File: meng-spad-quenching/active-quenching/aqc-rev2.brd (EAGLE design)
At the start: 120 x 74.9 mm, 297 parts, among them IC1 ADCMP582, IC10 74AHC1G04DBV, IC11 74AHC1G04DBV, IC12 TLV272DGK, IC13 TLV271DBV, IC14 74AHC1G04DBV, IC15 ALD1106, IC16 ALD1107, IC17 74AHC1G04DBV, IC18 LT1534-1, IC19 LT1534-1, IC2 TLV271DBV, IC20 STM32F411RE, IC22 TPS7A3001, IC24 TPS7A4901, IC25 TPS7A4901, IC27 USBLC6-2SC6Y, IC28 MAX572X, IC3 NC7SV74K8X, IC4 TLV272DGK, IC5 NC7WZ16P6X, IC6 LTC1711, IC7 DS1100LU-20+, IC8 LM1117, M1 BSS806N, M2 BSS806N, M3 BSS806N, Q1 IRLML6402TRPBF, Q2 MMBTH81, Q3 MMBTH81, Q5 MMBTH81, Q7 MMBTH81, Q8 MMBTH81, SW1 MCU_RST, T1 MMBTH10, T2 MMBTH10, T5 MMBTH10, T6 MMBTH10, T7 MMBTH10, T8 MMBTH10, T9 MMBTH10, U1 SN65EPT21DGK, U2 SN65EPT22DGK, X1 CONN_SPAD, X2 CONN_PHOTON_COUNTER, X3 KEYSTONE-7774, X4 KEYSTONE-7774, X5 CONN_SMU, X6 CONN_FORCE_QUENCH, X7 CONN_PULLDN_SENSE, X8 PN61729-S

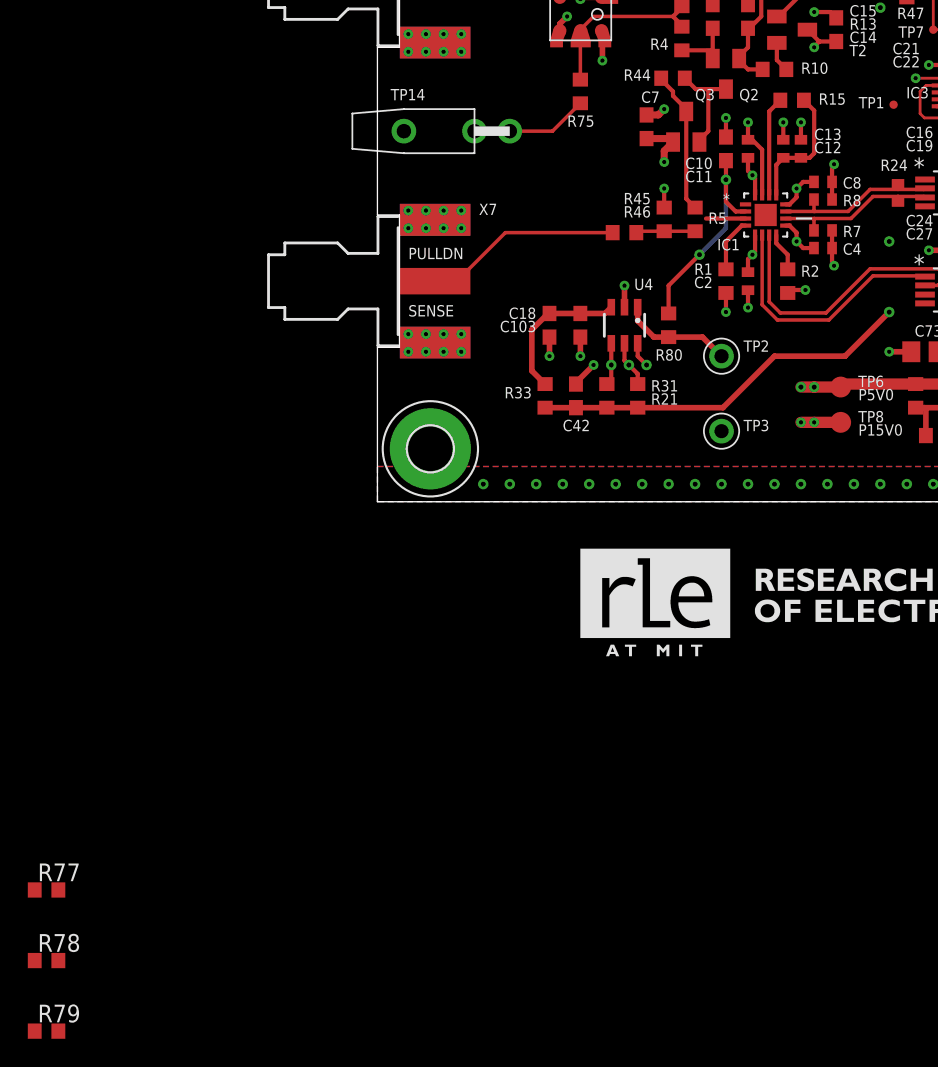
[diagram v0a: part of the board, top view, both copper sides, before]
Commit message: Placed and routed RC filter option
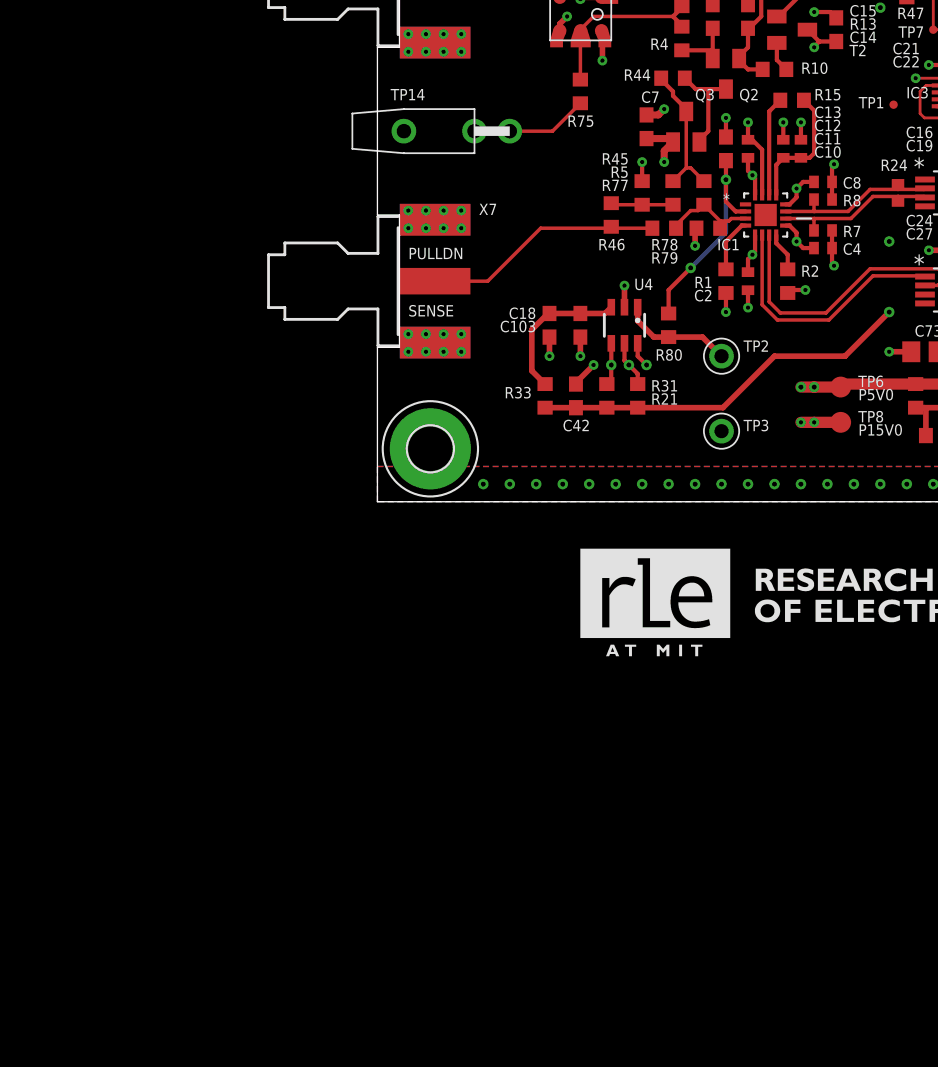
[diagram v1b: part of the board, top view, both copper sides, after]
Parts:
- moved R79 74.9 mm to (23.8, 19.7)
- moved R77 69.0 mm to (23.5, 22.2), turned to 90 degrees
- moved R78 68.9 mm to (20.6, 19.7)
- moved R45 2.48 mm to (19.1, 22.2)
- moved R5 2.48 mm to (21.3, 22.2)
- moved R46 1.59 mm to (16.8, 20.6), turned to 90 degrees
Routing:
- net SPAD_PULLDN_SENSE: track 2.85 -> 6.91 mm
- net N$32: track 14.2 -> 17.3 mm
- net GND: track 329.7 -> 331.0 mm, vias 357 -> 358

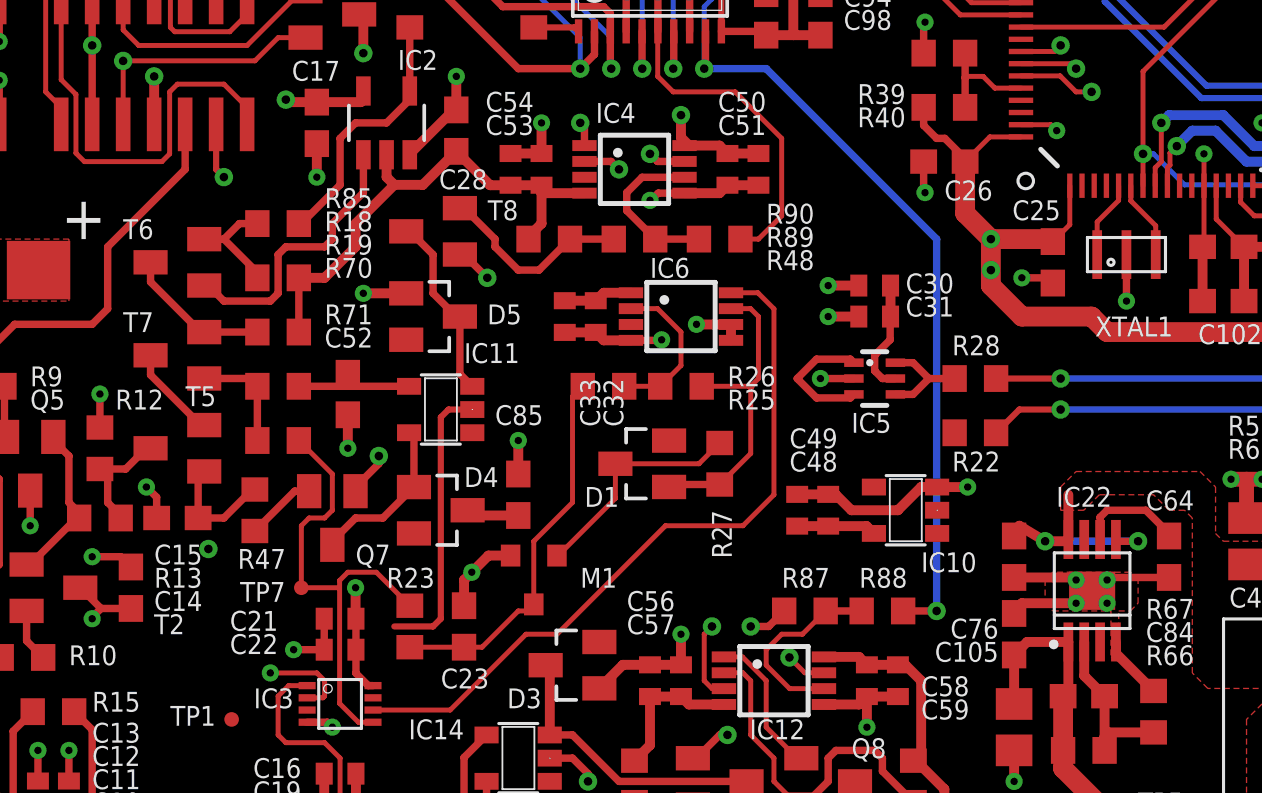
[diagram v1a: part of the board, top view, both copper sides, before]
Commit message: Misc routing, connected -5V to LDO output
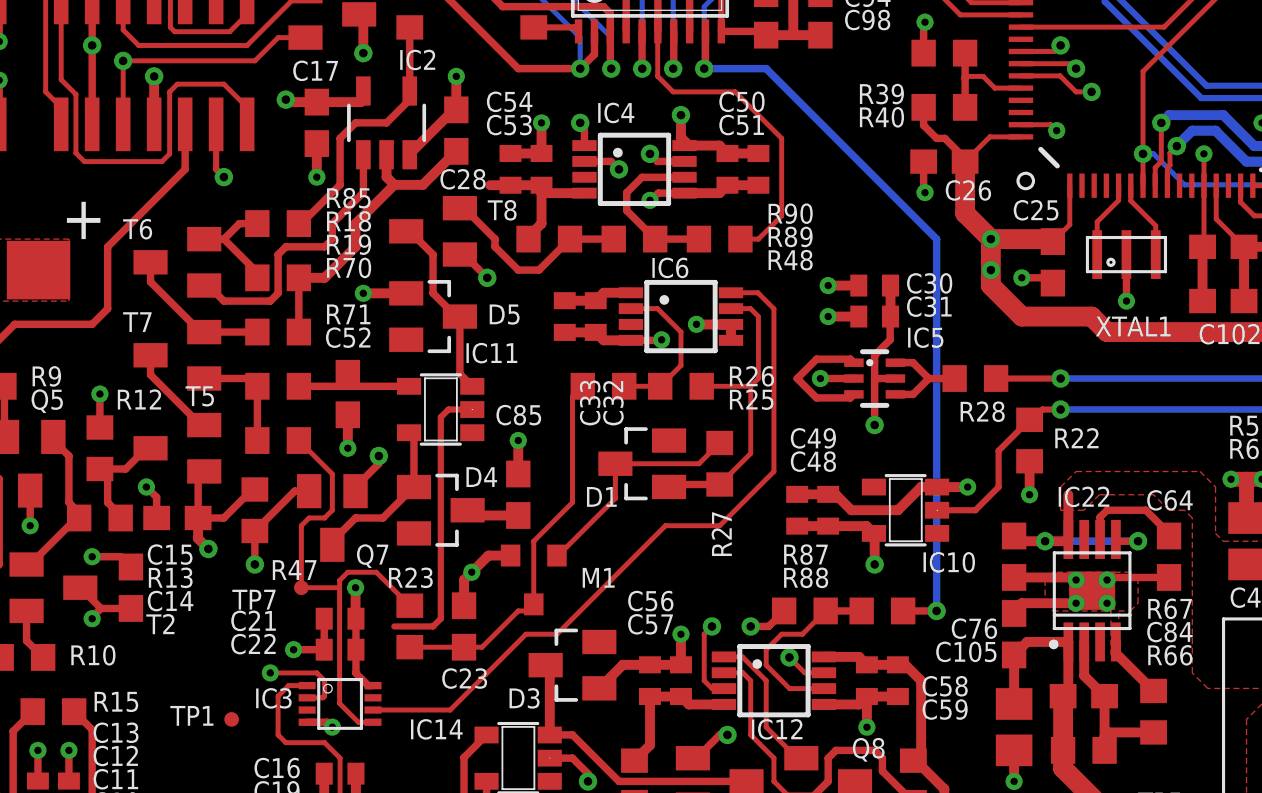
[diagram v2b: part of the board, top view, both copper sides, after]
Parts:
- moved R22 2.25 mm to (69.8, 40.0), turned to 90 degrees
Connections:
- net PP_N5V0: no longer C28.1, IC2.2, R18.1, R19.1
- net PP_N5V0_ANALOG: now also C28.1, IC2.2, R18.1, R19.1
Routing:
- net N$1: track 4.45 -> 29.5 mm, vias 1 -> 2
- net PP_N5V0: track 36.5 -> 21.7 mm
- net PP_P3V3: track 357.8 -> 371.9 mm, vias 16 -> 18
- net PP_N5V0_ANALOG: track 12.3 -> 25.1 mm
- net FORCE_QUENCH: track 71.9 -> 76.5 mm
- net PP_P5V0_ANALOG: track 192.6 -> 191.0 mm
- net GND: track 331.0 -> 332.4 mm, vias 358 -> 359
- net !ONE_SHOT_CLR: track 29.7 -> 29.2 mm

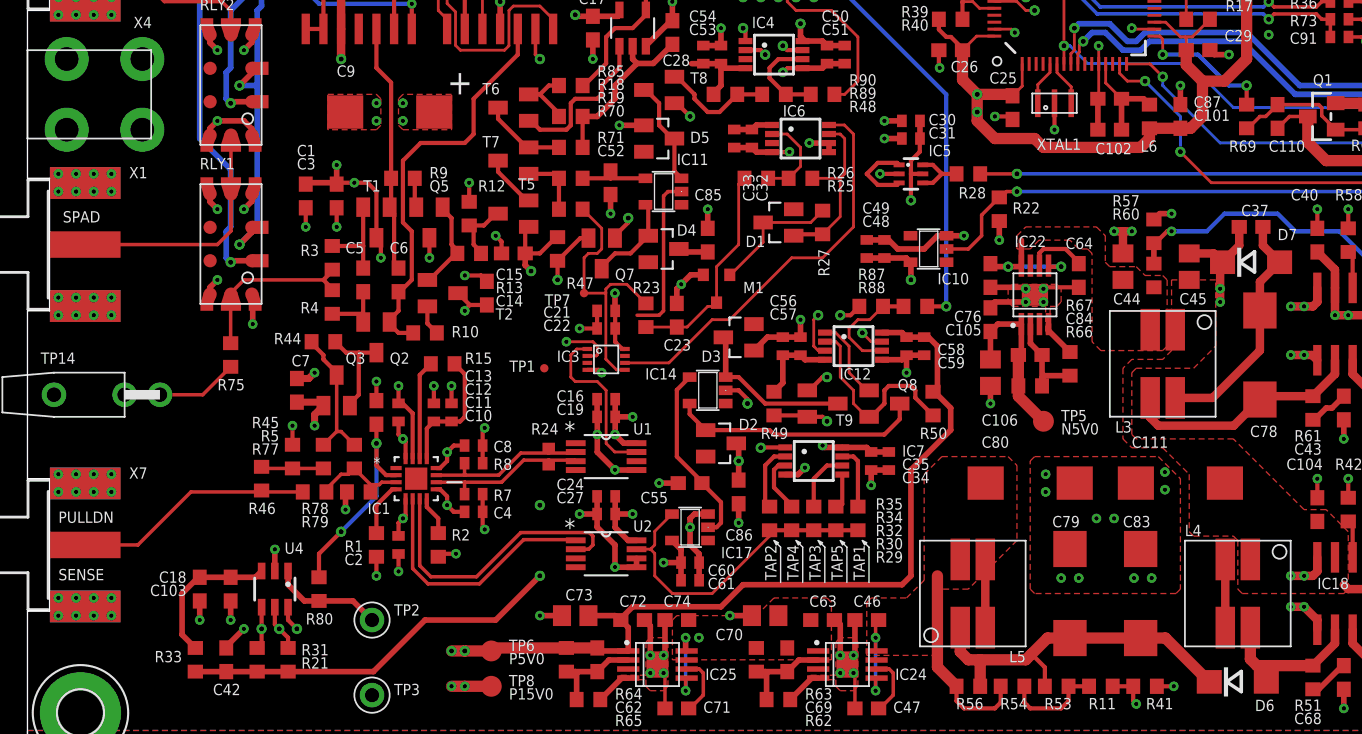
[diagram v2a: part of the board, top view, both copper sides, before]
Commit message: Routed relay power trace
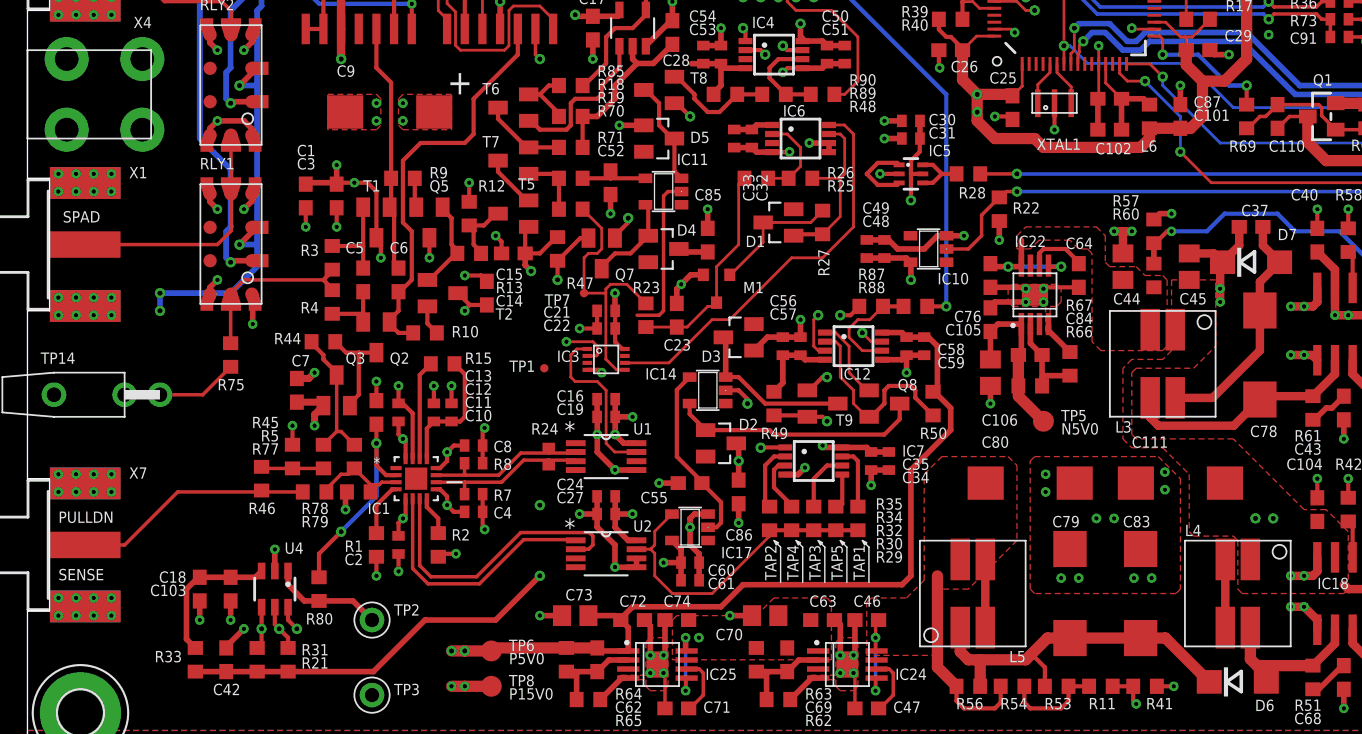
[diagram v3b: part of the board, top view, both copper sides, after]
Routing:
- net SMPS_USB_VDD: track 120.9 -> 253.9 mm, vias 6 -> 10
- net DAC2_SCL: track 162.3 -> 160.9 mm
- net DAC2_ADDRSEL: track 163.2 -> 161.8 mm
- net DAC2_SDA: track 160.6 -> 159.2 mm
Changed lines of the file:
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@@
 <contactref element="R78" pad="1"/>
 <wire x1="16.861078125" y1="19.685" x2="19.7875" y2="19.685" width="0.254" layer="1"/>
-<wire x1="16.861078125" y1="19.685" x2="11.7475" y2="19.685" width="0.254" layer="1"/>
-<wire x1="11.7475" y1="19.685" x2="7.9375" y2="15.875" width="0.254" layer="1"/>
-<wire x1="7.9375" y1="15.875" x2="4.1529" y2="15.875" width="0.254" layer="1"/>
+<wire x1="16.861078125" y1="19.685" x2="10.795" y2="19.685" width="0.254" layer="1"/>
+<wire x1="10.795" y1="19.685" x2="6.985" y2="15.875" width="0.254" layer="1"/>
+<wire x1="6.985" y1="15.875" x2="4.1529" y2="15.875" width="0.254" layer="1"/>
 <wire x1="16.8275" y1="19.7875" x2="16.8275" y2="19.718578125" width="0.254" layer="1"/>
 <wire x1="16.8275" y1="19.718578125" x2="16.861078125" y2="19.685" width="0.254" layer="1"/>
@@
 <wire x1="16.38" y1="13.55" x2="16.83" y2="14" width="0.4064" layer="1"/>
 <wire x1="12.3825" y1="13.55" x2="12.28" y2="13.55" width="0.4064" layer="1"/>
-<wire x1="12.28" y1="13.55" x2="11.1125" y2="12.3825" width="0.4064" layer="1"/>
-<wire x1="11.1125" y1="12.3825" x2="11.1125" y2="9.4225" width="0.4064" layer="1"/>
-<wire x1="11.1125" y1="9.4225" x2="12.065" y2="8.47" width="0.4064" layer="1"/>
+<wire x1="12.28" y1="13.55" x2="11.43" y2="12.7" width="0.4064" layer="1"/>
+<wire x1="11.43" y1="12.7" x2="11.43" y2="9.105" width="0.4064" layer="1"/>
+<wire x1="11.43" y1="9.105" x2="12.065" y2="8.47" width="0.4064" layer="1"/>
 </signal>
 <signal name="MCU_VCAP_2">
@@
 <wire x1="66.675" y1="71.12" x2="13.0175" y2="71.12" width="0.2032" layer="15"/>
 <wire x1="13.0175" y1="71.12" x2="12.3825" y2="70.485" width="0.2032" layer="15"/>
-<wire x1="12.3825" y1="17.78" x2="10.16" y2="15.5575" width="0.2032" layer="15"/>
-<wire x1="10.16" y1="15.5575" x2="10.16" y2="5.715" width="0.2032" layer="15"/>
-<wire x1="10.16" y1="5.715" x2="11.43" y2="4.445" width="0.2032" layer="15"/>
-<wire x1="11.43" y1="4.445" x2="16.1925" y2="4.445" width="0.2032" layer="15"/>
-<wire x1="16.1925" y1="4.445" x2="17.4625" y2="5.715" width="0.2032" layer="15"/>
+<wire x1="12.3825" y1="17.145" x2="10.795" y2="15.5575" width="0.2032" layer="15"/>
+<wire x1="10.795" y1="15.5575" x2="10.795" y2="5.715" width="0.2032" layer="15"/>
+<wire x1="10.795" y1="5.715" x2="11.43" y2="5.08" width="0.2032" layer="15"/>
+<wire x1="11.43" y1="5.08" x2="16.8275" y2="5.08" width="0.2032" layer="15"/>
+<wire x1="16.8275" y1="5.08" x2="17.4625" y2="5.715" width="0.2032" layer="15"/>
 <wire x1="17.4625" y1="5.715" x2="17.4625" y2="9.2075" width="0.2032" layer="15"/>
 <wire x1="17.4625" y1="9.2075" x2="16.8275" y2="9.8425" width="0.2032" layer="15"/>
-<wire x1="12.3825" y1="70.485" x2="12.3825" y2="17.78" width="0.2032" layer="15"/>
+<wire x1="12.3825" y1="70.485" x2="12.3825" y2="17.145" width="0.2032" layer="15"/>
 </signal>
 <signal name="DAC2_SCL">
@@
 <wire x1="11.7475" y1="70.8025" x2="12.7" y2="71.755" width="0.2032" layer="15"/>
 <wire x1="18.0975" y1="9.8425" x2="18.0975" y2="5.3975" width="0.2032" layer="15"/>
-<wire x1="18.0975" y1="5.3975" x2="16.51" y2="3.81" width="0.2032" layer="15"/>
-<wire x1="16.51" y1="3.81" x2="11.1125" y2="3.81" width="0.2032" layer="15"/>
-<wire x1="11.1125" y1="3.81" x2="9.525" y2="5.3975" width="0.2032" layer="15"/>
-<wire x1="9.525" y1="5.3975" x2="9.525" y2="15.875" width="0.2032" layer="15"/>
-<wire x1="9.525" y1="15.875" x2="11.7475" y2="18.0975" width="0.2032" layer="15"/>
-<wire x1="11.7475" y1="18.0975" x2="11.7475" y2="70.8025" width="0.2032" layer="15"/>
+<wire x1="18.0975" y1="5.3975" x2="17.145" y2="4.445" width="0.2032" layer="15"/>
+<wire x1="17.145" y1="4.445" x2="11.1125" y2="4.445" width="0.2032" layer="15"/>
+<wire x1="11.1125" y1="4.445" x2="10.16" y2="5.3975" width="0.2032" layer="15"/>
+<wire x1="10.16" y1="5.3975" x2="10.16" y2="15.875" width="0.2032" layer="15"/>
+<wire x1="10.16" y1="15.875" x2="11.7475" y2="17.4625" width="0.2032" layer="15"/>
+<wire x1="11.7475" y1="17.4625" x2="11.7475" y2="70.8025" width="0.2032" layer="15"/>
 </signal>
 <signal name="DAC2_ADDRSEL">
@@
 <wire x1="18.73" y1="11.4" x2="18.73" y2="10.48" width="0.3048" layer="1"/>
 <wire x1="18.73" y1="10.48" x2="19.3675" y2="9.8425" width="0.3048" layer="1"/>
-<wire x1="11.1125" y1="18.415" x2="8.89" y2="16.1925" width="0.2032" layer="15"/>
-<wire x1="8.89" y1="16.1925" x2="8.89" y2="5.08" width="0.2032" layer="15"/>
-<wire x1="8.89" y1="5.08" x2="10.795" y2="3.175" width="0.2032" layer="15"/>
-<wire x1="10.795" y1="3.175" x2="16.8275" y2="3.175" width="0.2032" layer="15"/>
-<wire x1="16.8275" y1="3.175" x2="18.7325" y2="5.08" width="0.2032" layer="15"/>
+<wire x1="11.1125" y1="17.78" x2="9.525" y2="16.1925" width="0.2032" layer="15"/>
+<wire x1="9.525" y1="16.1925" x2="9.525" y2="5.08" width="0.2032" layer="15"/>
+<wire x1="9.525" y1="5.08" x2="10.795" y2="3.81" width="0.2032" layer="15"/>
+<wire x1="10.795" y1="3.81" x2="17.4625" y2="3.81" width="0.2032" layer="15"/>
+<wire x1="17.4625" y1="3.81" x2="18.7325" y2="5.08" width="0.2032" layer="15"/>
 <wire x1="18.7325" y1="5.08" x2="18.7325" y2="9.2075" width="0.2032" layer="15"/>
 <wire x1="18.7325" y1="9.2075" x2="19.3675" y2="9.8425" width="0.2032" layer="15"/>
-<wire x1="11.1125" y1="71.12" x2="11.1125" y2="18.415" width="0.2032" layer="15"/>
+<wire x1="11.1125" y1="71.12" x2="11.1125" y2="17.78" width="0.2032" layer="15"/>
 </signal>
 <signal name="MCU_USB_FS_D_P" class="1">
@@
 <wire x1="16.1275" y1="50.1325" x2="16.1275" y2="49.7825" width="0.4064" layer="1"/>
 <wire x1="16.1275" y1="49.7825" x2="15.24" y2="48.895" width="0.4064" layer="1"/>
-<wire x1="15.24" y1="37.465" x2="16.51" y2="38.735" width="0.4064" layer="16"/>
-<wire x1="16.51" y1="38.735" x2="16.51" y2="48.839928125" width="0.4064" layer="16"/>
+<wire x1="15.24" y1="37.465" x2="16.51" y2="37.465" width="0.4064" layer="16"/>
+<wire x1="16.51" y1="37.465" x2="16.51" y2="48.839928125" width="0.4064" layer="16"/>
 <via x="13.335" y="63.8175" extent="1-16" drill="0.35" alwaysstop="yes"/>
 <wire x1="11.43" y1="66.255" x2="12.655" y2="66.255" width="0.4064" layer="1"/>
@@
 <wire x1="107.315" y1="15.24" x2="107.315" y2="32.385" width="0.8128" layer="1"/>
 <wire x1="107.315" y1="32.385" x2="105.41" y2="34.29" width="0.8128" layer="1"/>
-<wire x1="82.4975" y1="31.3425" x2="16.51" y2="38.735" width="0" layer="19" extent="1-16"/>
+<via x="88.265" y="17.78" extent="1-16" drill="0.35" alwaysstop="yes"/>
+<via x="89.535" y="17.78" extent="1-16" drill="0.35" alwaysstop="yes"/>
+<wire x1="89.535" y1="17.78" x2="88.265" y2="17.78" width="0.8128" layer="15"/>
+<wire x1="73.025" y1="2.54" x2="88.265" y2="17.78" width="0.8128" layer="15"/>
+<wire x1="16.51" y1="37.465" x2="16.51" y2="35.8775" width="0.4064" layer="16"/>
+<wire x1="16.51" y1="35.8775" x2="14.605" y2="33.9725" width="0.4064" layer="16"/>
+<wire x1="9.525" y1="33.9725" x2="14.605" y2="33.9725" width="0.4064" layer="16"/>
+<via x="9.525" y="33.9725" extent="1-16" drill="0.35" alwaysstop="yes"/>
+<via x="9.525" y="32.7025" extent="1-16" drill="0.35" alwaysstop="yes"/>
+<wire x1="9.525" y1="32.7025" x2="9.525" y2="33.9725" width="0.4064" layer="16"/>
+<wire x1="9.525" y1="33.9725" x2="9.525" y2="32.7025" width="0.8128" layer="15"/>
+<wire x1="9.525" y1="32.7025" x2="4.445" y2="27.6225" width="0.8128" layer="15"/>
+<wire x1="4.445" y1="27.6225" x2="4.445" y2="26.035" width="0.8128" layer="15"/>
+<wire x1="4.445" y1="26.035" x2="8.255" y2="22.225" width="0.8128" layer="15"/>
+<wire x1="8.255" y1="22.225" x2="8.255" y2="4.445" width="0.8128" layer="15"/>
+<wire x1="8.255" y1="4.445" x2="10.16" y2="2.54" width="0.8128" layer="15"/>
+<wire x1="10.16" y1="2.54" x2="73.025" y2="2.54" width="0.8128" layer="15"/>
 </signal>
 <signal name="!MCU_SMPS_PRECHG">
